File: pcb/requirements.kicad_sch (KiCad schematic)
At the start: 10 parts

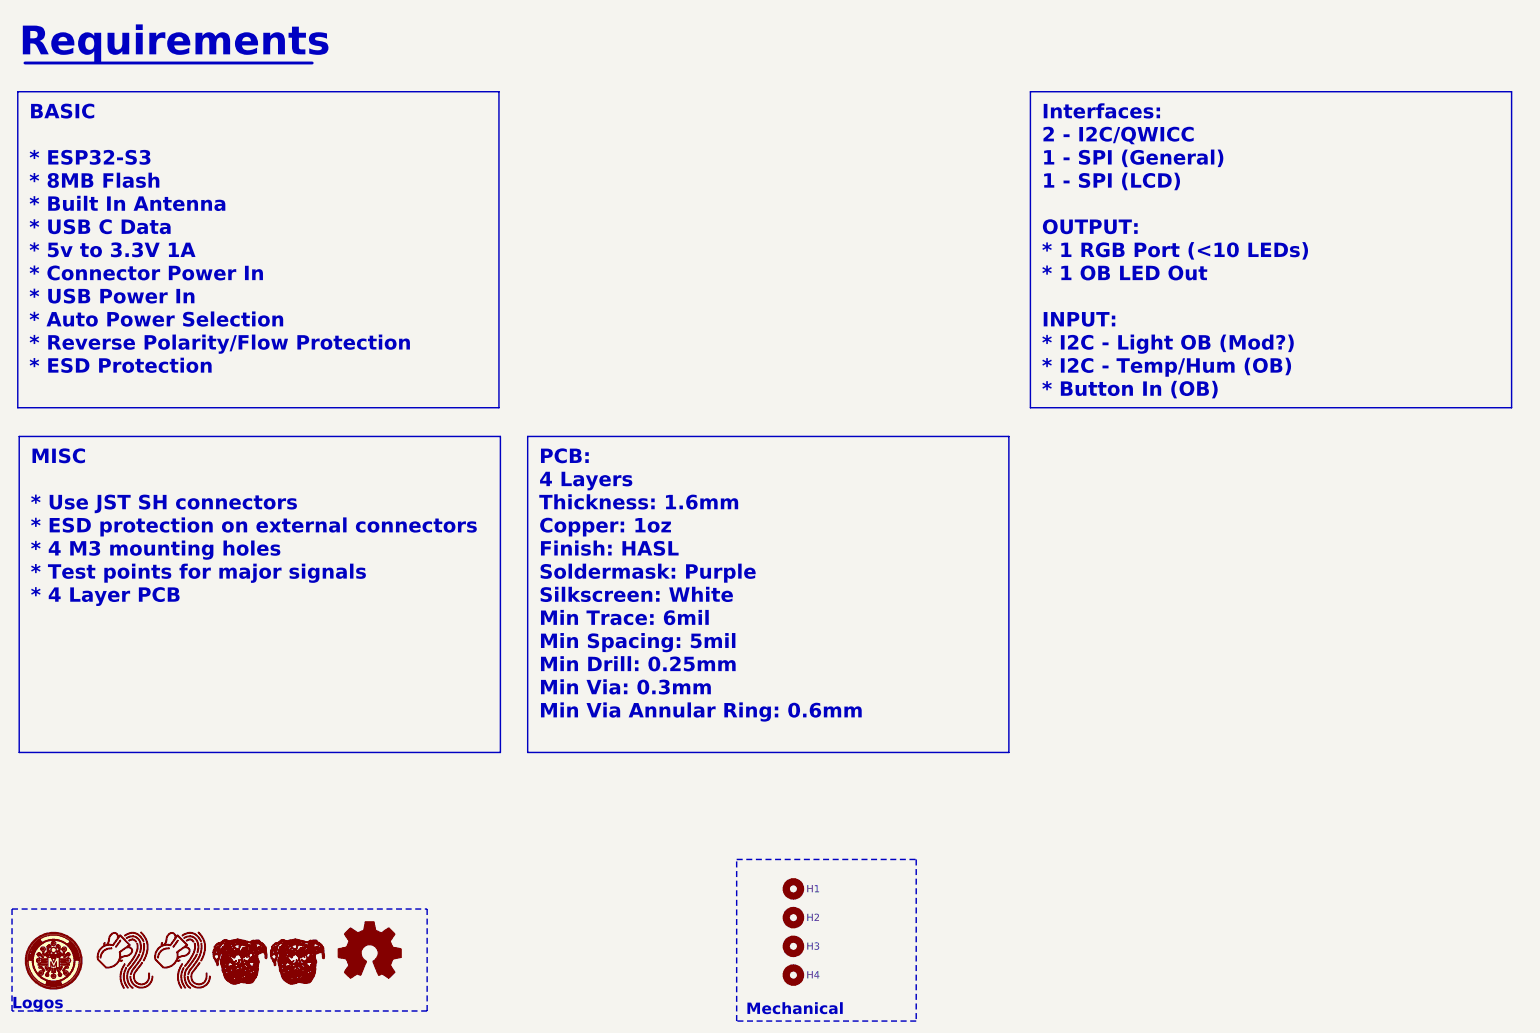
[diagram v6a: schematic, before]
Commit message: Updated part attributes for consistency.
Updated requirements section to be more accurate.
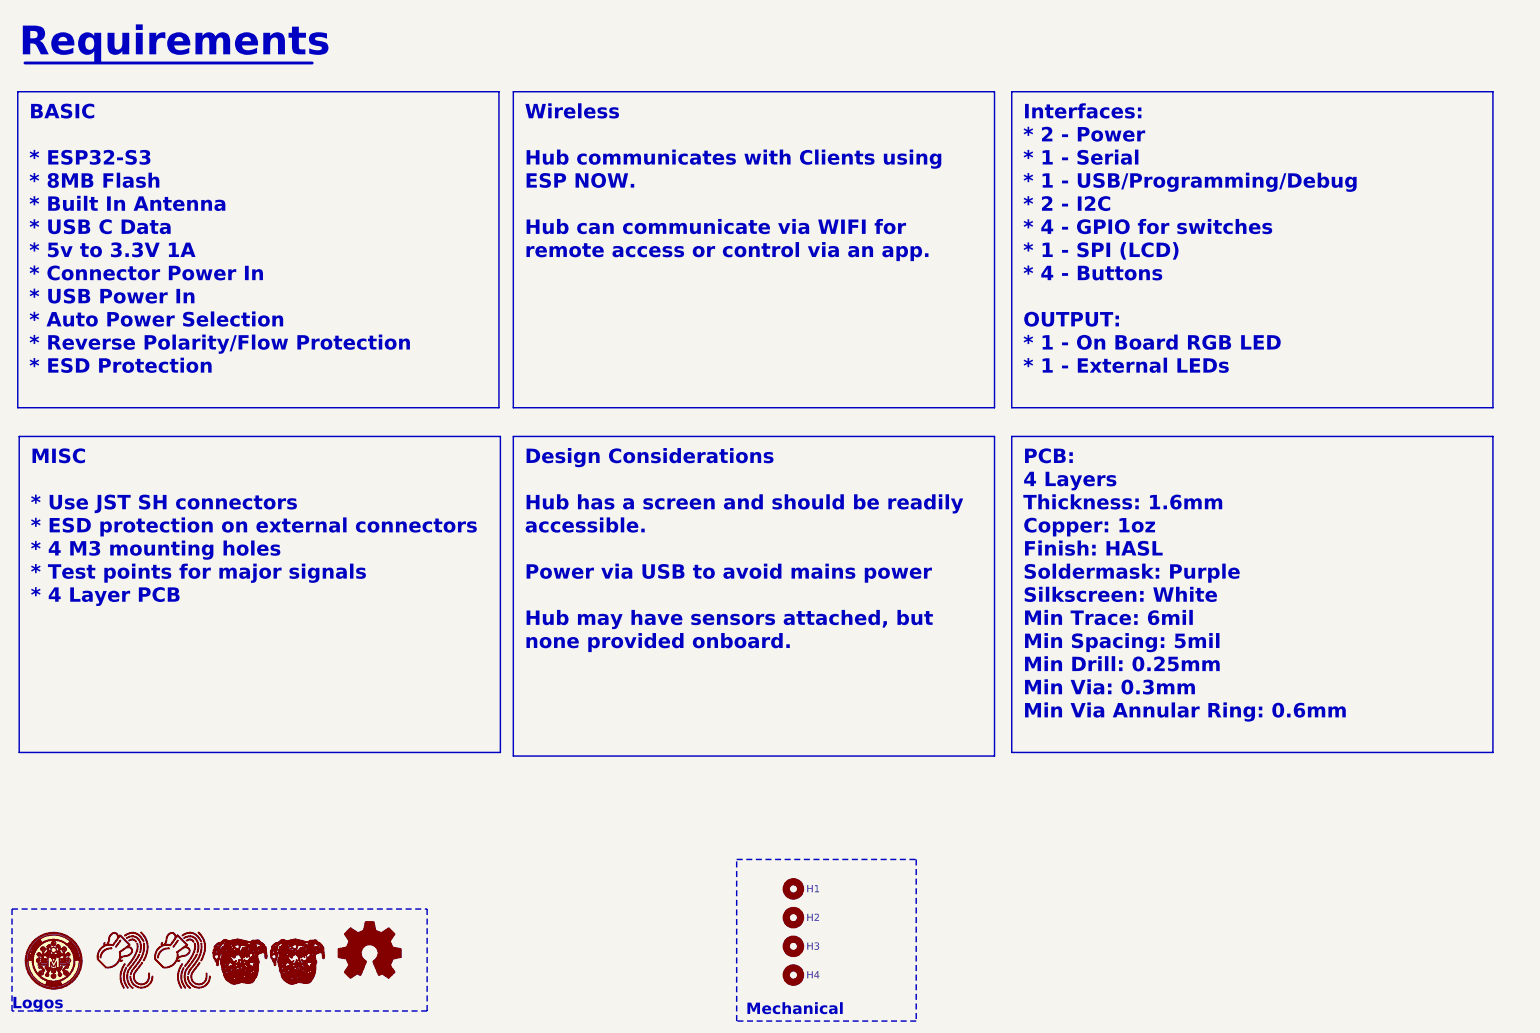
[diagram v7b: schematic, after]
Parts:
- LOGO1: now left out of the parts list
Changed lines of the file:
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@@
+		)
+	)
+	(text_box "Design Considerations\n\nHub has a screen and should be readily accessible.\n\nPower via USB to avoid mains power\n\nHub may have sensors attached, but none provided onboard.\n"
+		(exclude_from_sim yes)
+		(at 104.14 91.44 0)
+		(size 85.09 56.515)
+		(margins 2.032 2.032 2.032 2.032)
+		(stroke
+			(width 0.254)
+			(type solid)
+			(color 132 0 132 1)
+		)
+		(fill
+			(type color)
+			(color 255 229 191 1)
+		)
+		(effects
+			(font
+				(size 2.54 2.54)
+				(thickness 0.254)
+				(bold yes)
+				(color 194 0 194 1)
+			)
+			(justify left top)
 		)
 	)
@@
 		)
 	)
+	(text_box "Wireless\n\nHub communicates with Clients using ESP NOW. \n\nHub can communicate via WIFI for remote access or control via an app.\n\n"
+		(exclude_from_sim yes)
+		(at 104.14 30.48 0)
+		(size 85.09 55.88)
+		(margins 2.032 2.032 2.032 2.032)
+		(stroke
+			(width 0.254)
+			(type solid)
+			(color 132 0 132 1)
+		)
+		(fill
+			(type color)
+			(color 255 229 191 1)
+		)
+		(effects
+			(font
+				(size 2.54 2.54)
+				(thickness 0.254)
+				(bold yes)
+				(color 194 0 194 1)
+			)
+			(justify left top)
+		)
+	)
 	(text_box "PCB:\n4 Layers\nThickness: 1.6mm\nCopper: 1oz\nFinish: HASL\nSoldermask: Purple\nSilkscreen: White\nMin Trace: 6mil\nMin Spacing: 5mil\nMin Drill: 0.25mm\nMin Via: 0.3mm\nMin Via Annular Ring: 0.6mm\n\n"
 		(exclude_from_sim yes)
-		(at 106.68 91.44 0)
-		(size 85.09 55.88)
-		(margins 2.032 2.032 2.032 2.032)
-		(stroke
-			(width 0.254)
-			(type solid)
-			(color 132 0 132 1)
-		)
-		(fill
-			(type color)
-			(color 255 229 191 1)
-		)
-		(effects
-			(font
-				(size 2.54 2.54)
-				(thickness 0.254)
-				(bold yes)
-				(color 194 0 194 1)
-			)
-			(justify left top)
-		)
-	)
-	(text_box "Interfaces:\n2 - I2C/QWICC\n1 - SPI (General)\n1 - SPI (LCD)\n\nOUTPUT:\n* 1 RGB Port (<10 LEDs)\n* 1 OB LED Out\n\nINPUT:\n* I2C - Light OB (Mod?)\n* I2C - Temp/Hum (OB)\n* Button In (OB)"
-		(exclude_from_sim yes)
-		(at 195.58 30.48 0)
+		(at 192.278 91.44 0)
+		(size 85.09 55.88)
+		(margins 2.032 2.032 2.032 2.032)
+		(stroke
+			(width 0.254)
+			(type solid)
+			(color 132 0 132 1)
+		)
+		(fill
+			(type color)
+			(color 255 229 191 1)
+		)
+		(effects
+			(font
+				(size 2.54 2.54)
+				(thickness 0.254)
+				(bold yes)
+				(color 194 0 194 1)
+			)
+			(justify left top)
+		)
+	)
+	(text_box "Interfaces:\n* 2 - Power\n* 1 - Serial\n* 1 - USB/Programming/Debug\n* 2 - I2C\n* 4 - GPIO for switches\n* 1 - SPI (LCD)\n* 4 - Buttons\n\nOUTPUT:\n* 1 - On Board RGB LED\n* 1 - External LEDs"
+		(exclude_from_sim yes)
+		(at 192.278 30.48 0)
 		(size 85.09 55.88)
 		(margins 2.032 2.032 2.032 2.032)
@@
 		(unit 1)
 		(exclude_from_sim no)
-		(in_bom yes)
+		(in_bom no)
 		(on_board yes)
 		(dnp no)
@@
 			(at 22.86 184.15 0)
 			(effects
+				(font
+					(size 1.27 1.27)
+				)
+				(hide yes)
+			)
+		)
+		(property "LCSC" ""
+			(at 22.86 184.15 0)
+			(effects
+				(font
+					(size 1.27 1.27)
+				)
+				(hide yes)
+			)
+		)
+		(property "Digikey" ""
+			(at 22.86 184.15 0)
+			(effects
+				(font
+					(size 1.27 1.27)
+				)
+				(hide yes)
+			)
+		)
+		(property "Mouser" ""
+			(at 22.86 184.15 0)
+			(effects

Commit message: Moved connectors
Moved I2C to edge
Rearranged all GPIO
Re-routed as necessary
(I don't like the button connector layout -- like the old way more)
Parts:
- LOGO5: footprint CRGM Logos:Roxy 6.5mm -> CRGM Logos:Roxy 8mm
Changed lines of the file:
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@@
 			)
 		)
-		(property "Footprint" "CRGM Logos:Roxy 6.5mm"
+		(property "Footprint" "CRGM Logos:Roxy 8mm"
 			(at 55.88 192.278 0)
 			(effects
